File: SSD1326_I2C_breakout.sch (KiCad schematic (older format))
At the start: 23 parts, among them J1 Conn_01x04, U1 MAX607ESA-T, U2 ER-OLED018-1, U3 APX803, U4 AP2112K-3.3

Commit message: adding images and such
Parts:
- J1: footprint Connector_PinSocket_2.54mm:PinSocket_1x04_P2.54mm_Vertical -> onigaku:PinSocket_1x04_P2.54mm_Vertical
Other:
- note added: "12V and 3.3V Power Supply"
- note added: "SSD1326 / ER-OLED018-1"
- note removed: "15V and 3.3V Power Supply"
- moved on the sheet: C10, C11, C7, C8, C9, R1, R2, R3, U2

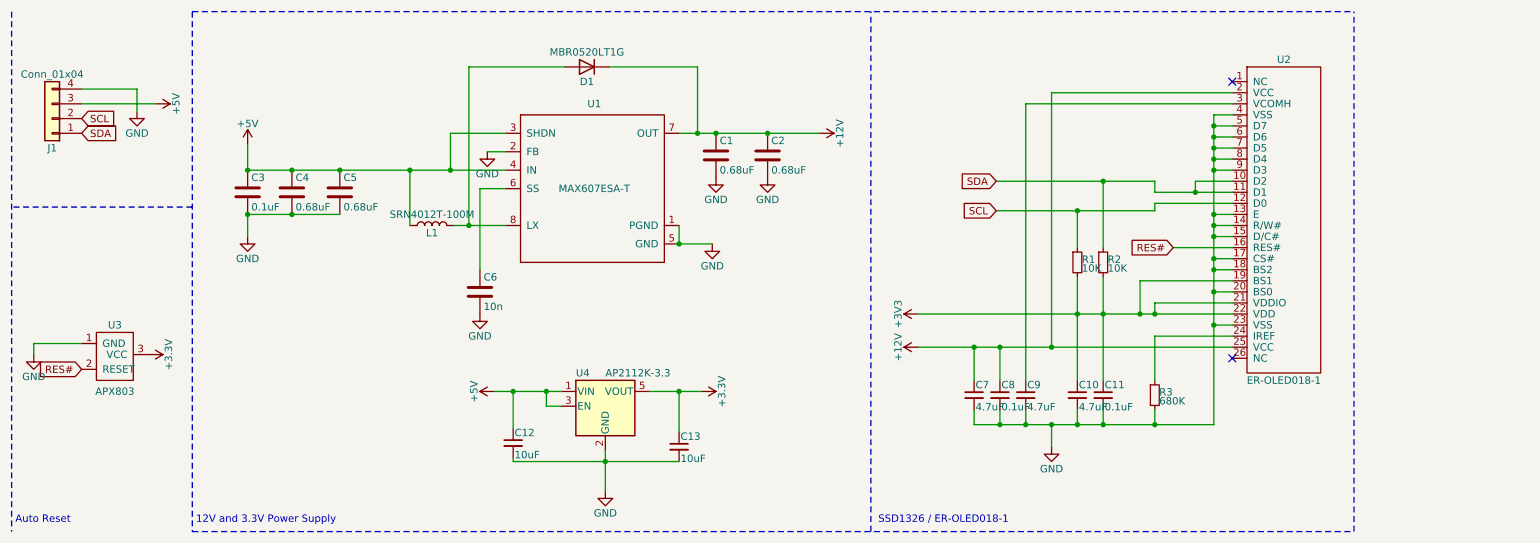
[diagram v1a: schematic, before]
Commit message: swapped out max607 for a max8570 due to cost savings and obsoletion, using B0520LW schottky due to similar circumstances
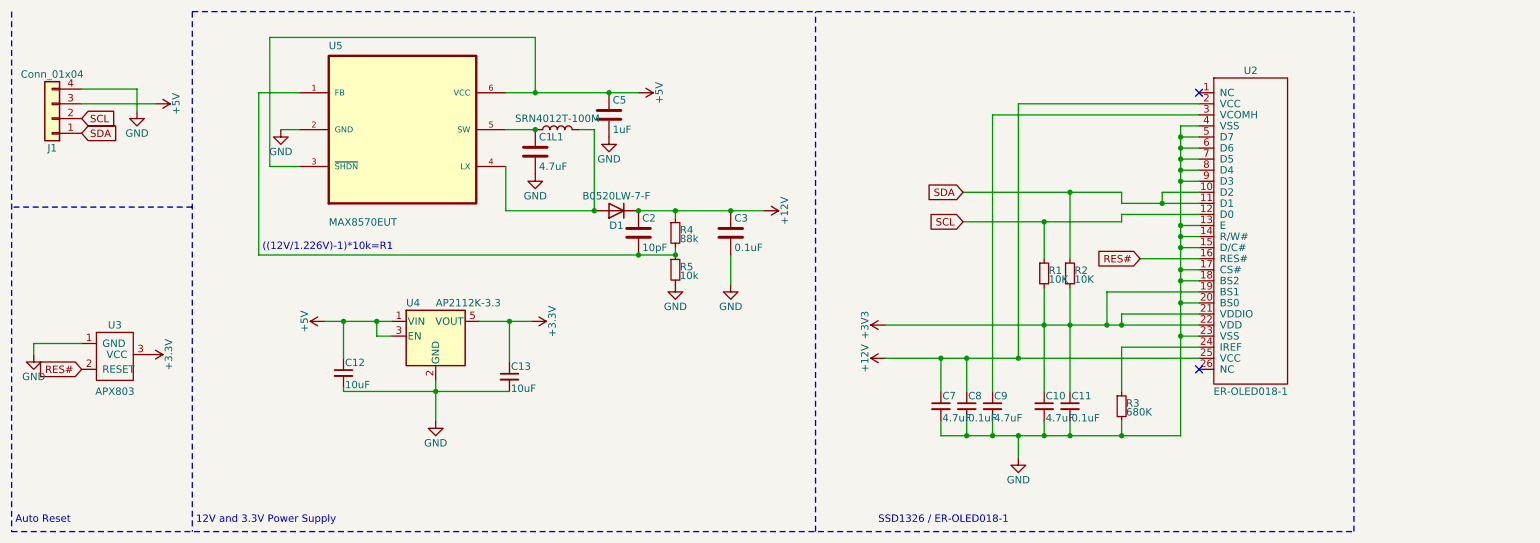
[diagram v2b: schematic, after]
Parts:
- removed C4: 0.68uF, Capacitor_SMD:C_0603_1608Metric_Pad1.08x0.95mm_HandSolder, symbol Device:C
- removed C6: 10n, Capacitor_SMD:C_0603_1608Metric_Pad1.08x0.95mm_HandSolder, symbol Device:C
- removed U1: MAX607ESA-T, onigaku:max607esa&plus_T, symbol onigaku:MAX607ESA-T
- added R4: 88k, Resistor_SMD:R_0603_1608Metric_Pad0.98x0.95mm_HandSolder, symbol Device:R_Small
- added R5: 10k, Resistor_SMD:R_0603_1608Metric_Pad0.98x0.95mm_HandSolder, symbol Device:R_Small
- added U5: MAX8570EUT, onigaku:MAX8570EUT+SOT95P280X145-6N, symbol max8570:MAX8570EUT
- C1: value 0.68uF -> 4.7uF
- C2: value 0.68uF -> 10pF
- C5: value 0.68uF -> 1uF
- D1: value MBR0520LT1G -> ‎B0520LW-7-F‎; footprint onigaku:MBR0520LT1G -> onigaku:B0520LW
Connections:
- net +12V: now also C3.1, R4.1; no longer C1.1
- net +5V: now also U5.3 (~SHDN), U5.6 (VCC); no longer C3.1, L1.1
- net GND: now also R5.2, U5.2 (GND); no longer C2.2
- net at D1.2 (A), L1.2: now also U5.4 (LX)
- new net: C1.1, L1.1, U5.5 (SW)
- new net: C2.2, R4.2, R5.1, U5.1 (FB)
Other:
- note added: "((12V/1.226V)-1)*10k=R1"
- moved on the sheet: C1, C10, C11, C12, C13, C2, C3, C5, C7, C8, C9, D1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

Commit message: slimming down to 12mm
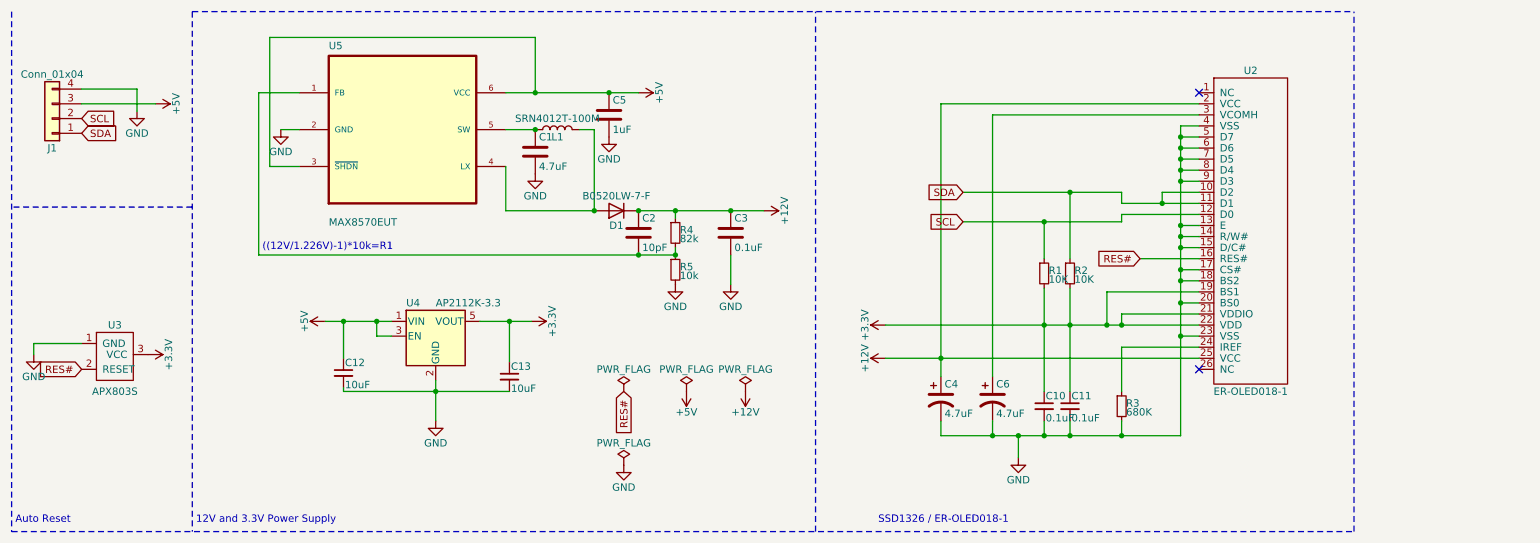
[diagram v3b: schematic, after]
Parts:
- removed C7, C9: 4.7uF, Capacitor_SMD:C_0603_1608Metric_Pad1.08x0.95mm_HandSolder, symbol Device:C_Small
- removed C8: 0.1uF, Capacitor_SMD:C_0603_1608Metric_Pad1.08x0.95mm_HandSolder, symbol Device:C_Small
- added C4, C6: 4.7uF, Capacitor_Tantalum_SMD:CP_EIA-2012-15_AVX-P_Pad1.30x1.05mm_HandSolder, symbol Device:CP1
- C10: value 4.7uF -> 0.1uF
- J1: footprint onigaku:PinSocket_1x04_P2.54mm_Vertical -> kbd:OLED
- R4: value 88k -> 82k
- U3: value APX803 -> APX803S; footprint onigaku:APX803-SOT91P240X110-3N -> onigaku:APX803S-SA-SOT91P240X110-3N
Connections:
- net +12V: now also C4.1
- net GND: now also C4.2, C6.2
- net at U2.3 (VCOMH): now also C6.1
